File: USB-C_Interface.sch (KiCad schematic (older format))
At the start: 66 parts, among them IC3 TPS7A0518PDBVT, J12 WE_632723300011, J3 WE_632723300011, J4 WE_632723300011, U5 TPS25820DSST, U6 TS3USB30EDGSR, U7 TXB0104D, U8 CBTL02043ABQ,115, U9 FT232RQ-REEL

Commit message: Update power labels in USB2 seciton of USB sch, reorganize USB2 section
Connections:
- net labels added: 1V8_SYS, 3V3_SYS, 5V_SYS, VREG_S4A_1V8
- wire segments 309 -> 306
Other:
- moved on the sheet: C60, C61, C62, C63, C69, C70, C71, C72, C73, C74, C75, C80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

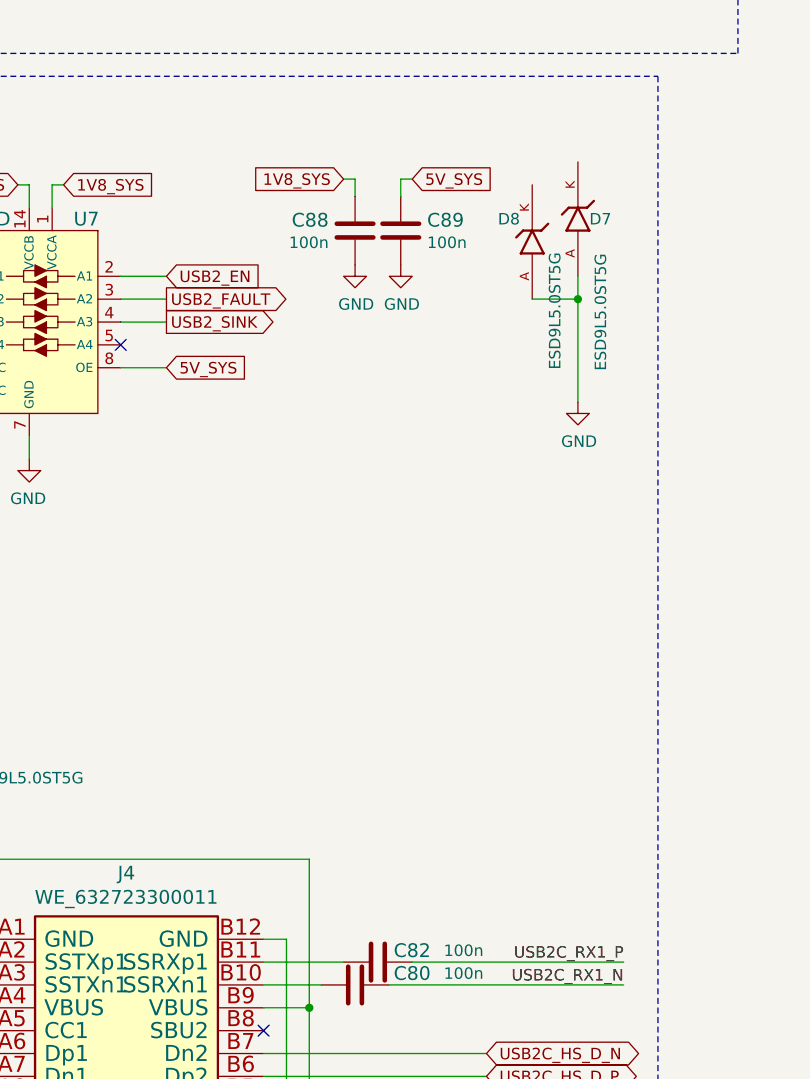
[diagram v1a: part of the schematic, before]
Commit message: Change U7 OE voltage to 1V8, change USB2.0 TSV to TPD4E05U06 to consolidate bom
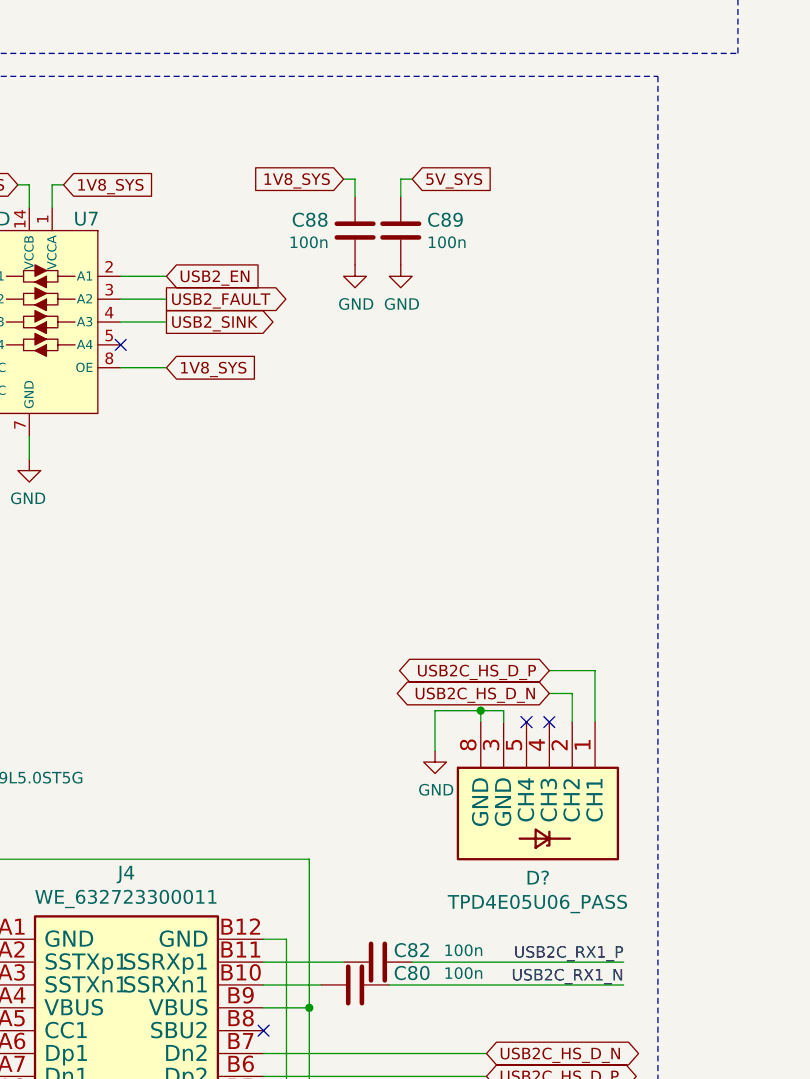
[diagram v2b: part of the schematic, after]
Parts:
- removed D7, D8: ESD9L5.0ST5G, sa800u-baseboard-hw-footprints:DIOM1006X40N, symbol sa800u-baseboard-hw:ESD9L5.0ST5G
- added D?: TPD4E05U06_PASS, sa800u-baseboard-hw-footprints:TPD4E05U06_PASS, symbol sa800u-baseboard-hw:TPD4E05U06_PASS
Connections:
- wire segments 306 -> 312
- no-connect marks 32 -> 34
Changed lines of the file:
@@
 Text Label 10700 9675 2    50   ~ 0
 USB2C_TX2_N
-$Comp
-L sa800u-baseboard-hw:ESD9L5.0ST5G D8
-U 1 1 62A14876
-P 10300 5725
-AR Path="/61A2F307/62A14876" Ref="D8"  Part="1"
-AR Path="/628CDA4A/62A14876" Ref="D?"  Part="1"
-F 0 "D8" V 10400 5875 50  0000 R CNN
-F 1 "ESD9L5.0ST5G" H 10255 5625 50  0000 R CNN
-F 2 "sa800u-baseboard-hw-footprints:DIOM1006X40N" H 10050 5925 50  0001 C CNN
-F 3 "https://www.farnell.com/datasheets/2353986.pdf" H 10300 5725 50  0001 C CNN
-F 4 "ESD9L5.0ST5G" H 10000 5975 50  0001 C CNN "MPN"
-F 5 "ONSEMI" H 10450 5975 50  0001 C CNN "Manufacturer"
-	1    10300 5725
-	0    -1   -1   0
-$EndComp
-$Comp
-L sa800u-baseboard-hw:ESD9L5.0ST5G D7
-U 1 1 62A1487E
-P 10500 5625
-AR Path="/61A2F307/62A1487E" Ref="D7"  Part="1"
-AR Path="/628CDA4A/62A1487E" Ref="D?"  Part="1"
-F 0 "D7" V 10500 5575 50  0000 R CNN
-F 1 "ESD9L5.0ST5G" H 10350 5525 50  0000 R CNN
-F 2 "sa800u-baseboard-hw-footprints:DIOM1006X40N" H 10250 5825 50  0001 C CNN
-F 3 "https://www.farnell.com/datasheets/2353986.pdf" H 10500 5625 50  0001 C CNN
-F 4 "ESD9L5.0ST5G" H 10200 5875 50  0001 C CNN "MPN"
-F 5 "ONSEMI" H 10650 5875 50  0001 C CNN "Manufacturer"
-	1    10500 5625
-	0    -1   -1   0
-$EndComp
-Wire Wire Line
-	10500 5875 10500 5975
-Wire Wire Line
-	10300 5975 10500 5975
-Connection ~ 10500 5975
-Wire Wire Line
-	10500 5975 10500 6425
-$Comp
-L sa800u-baseboard-hw:GND #PWR039
-U 1 1 62A1488A
-P 10500 6425
-AR Path="/61A2F307/62A1488A" Ref="#PWR039"  Part="1"
-AR Path="/628CDA4A/62A1488A" Ref="#PWR?"  Part="1"
-F 0 "#PWR039" H 10500 6175 50  0001 C CNN
-F 1 "GND" H 10505 6252 50  0000 C CNN
-F 2 "" H 10500 6425 50  0001 C CNN
-F 3 "" H 10500 6425 50  0001 C CNN
-	1    10500 6425
-	1    0    0    -1
-$EndComp
 Wire Wire Line
 	6975 9375 7925 9375
@@
 Wire Wire Line
 	8250 5475 8200 5475
-Text GLabel 8700 6275 2    50   Input ~ 0
-5V_SYS
 Text GLabel 8050 5475 0    50   Input ~ 0
 5V_SYS
@@
 Wire Wire Line
 	9475 5450 9525 5450
+Text GLabel 8700 6275 2    50   Input ~ 0
+1V8_SYS
+$Comp
+L sa800u-baseboard-hw:TPD4E05U06_PASS D?
+U 1 1 63DB6B08
+P 10375 8025
+AR Path="/61C01D88/63DB6B08" Ref="D?"  Part="1"
+AR Path="/61A2F307/63DB6B08" Ref="D?"  Part="1"
+F 0 "D?" V 10858 7975 60  0000 C CNN
+F 1 "TPD4E05U06_PASS" V 10964 7975 60  0000 C CNN
+F 2 "sa800u-baseboard-hw-footprints:TPD4E05U06_PASS" H 10375 8025 60  0001 C CNN
+F 3 "" H 10375 8025 60  0001 C CNN
+F 4 "Texas Instruments" H 10375 8025 50  0001 C CNN "Manufacturer"
+F 5 "TPD4E05U06DQAR" H 10375 8025 50  0001 C CNN "MPN"
+	1    10375 8025
+	0    1    1    0
+$EndComp
+Wire Wire Line
+	10175 7825 10175 7775
+Wire Wire Line
+	10175 7775 10075 7775
+Wire Wire Line
+	9875 7775 9875 7950
+Wire Wire Line
+	10075 7825 10075 7775
+Connection ~ 10075 7775
+Wire Wire Line
+	10075 7775 9875 7775
+$Comp
+L sa800u-baseboard-hw:GND #PWR?
+U 1 1 63DB6B14
+P 9875 7950
+AR Path="/61A60486/63DB6B14" Ref="#PWR?"  Part="1"
+AR Path="/61C01D88/63DB6B14" Ref="#PWR?"  Part="1"
+AR Path="/61A2F307/63DB6B14" Ref="#PWR?"  Part="1"
+F 0 "#PWR?" H 9875 7700 50  0001 C CNN
+F 1 "GND" H 9880 7777 50  0000 C CNN
+F 2 "" H 9875 7950 50  0001 C CNN
+F 3 "" H 9875 7950 50  0001 C CNN
+	1    9875 7950
+	1    0    0    -1
+$EndComp
+Wire Wire Line
+	10375 7700 10475 7700
+Wire Wire Line
+	10475 7700 10475 7825
+Wire Wire Line
+	10375 7600 10575 7600
+Wire Wire Line
+	10575 7600 10575 7825
+NoConn ~ 10375 7825
+NoConn ~ 10275 7825
+Text GLabel 10375 7600 0    50   BiDi ~ 0
+USB2C_HS_D_P
+Text GLabel 10375 7700 0    50   BiDi ~ 0
+USB2C_HS_D_N
 $EndSCHEMATC

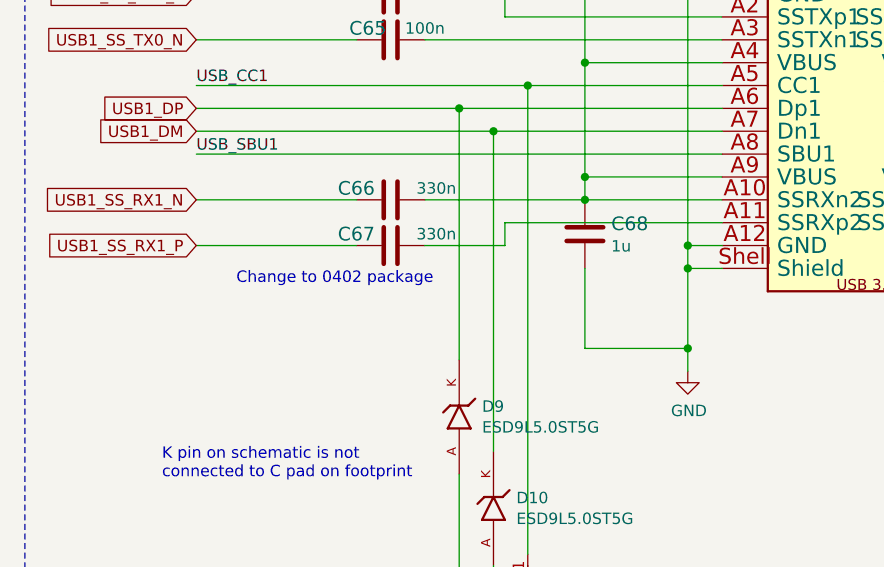
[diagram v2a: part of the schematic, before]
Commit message: Remove junction between USB1_SS_RX1_N and USB_VBUS
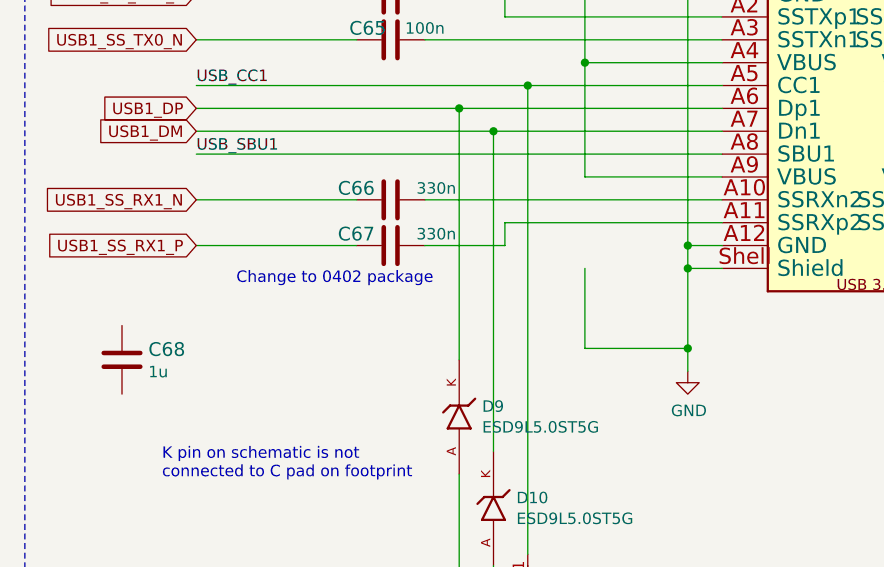
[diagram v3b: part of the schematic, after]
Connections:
- wire segments 312 -> 310
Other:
- moved on the sheet: C68
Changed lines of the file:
@@
 Wire Wire Line
 	5000 800  5000 1800
-$Comp
-L sa800u-baseboard-hw:C_1u_0402 C68
-U 1 1 61ACCBAB
-P 2950 2550
-F 0 "C68" H 3065 2595 60  0000 L CNN
-F 1 "C_1u_0402" H 2950 2400 60  0001 C CNN
-F 2 "sa800u-baseboard-hw-footprints:0402-cap" H 3150 2750 60  0001 L CNN
-F 3 "" H 2950 2550 50  0001 C CNN
-F 4 "TDK" H 3150 2950 60  0001 L CNN "Manufacturer"
-F 5 "C1005X6S1A105K050BC" H 3150 2850 60  0001 L CNN "MPN"
-F 6 "1u" H 3065 2497 50  0000 L CNN "Val"
-	1    2950 2550
-	1    0    0    -1
-$EndComp
 Wire Wire Line
 	3550 1800 2950 1800
@@
 	1    0    0    -1
 $EndComp
-Wire Wire Line
-	2950 2300 2950 2400
-Connection ~ 2950 2300
-Wire Wire Line
-	2950 2700 2950 3050
-Wire Wire Line
-	2950 3050 3400 3050
 Wire Wire Line
 	3550 1500 3400 1500
@@
 	1250 2200 3550 2200
 Wire Wire Line
-	3550 2400 2950 2400
-Connection ~ 2950 2400
-Wire Wire Line
-	2950 2400 2250 2400
-Wire Wire Line
 	3550 2500 2600 2500
 Wire Wire Line
@@
 Connection ~ 3400 2700
 Wire Wire Line
-	3400 2700 3400 3050
-Wire Wire Line
 	4800 2600 4800 3150
-Wire Wire Line
-	3400 3050 3400 3150
-Connection ~ 3400 3050
 $Comp
 L sa800u-baseboard-hw:TPD1E10B06DPYR D11
@@
 Text GLabel 10375 7700 0    50   BiDi ~ 0
 USB2C_HS_D_N
+Wire Wire Line
+	3400 3050 3400 3150
+Wire Wire Line
+	3400 2700 3400 3050
+Connection ~ 3400 3050
+Wire Wire Line
+	2950 3050 3400 3050
+Wire Wire Line
+	2950 2700 2950 3050
+$Comp
+L sa800u-baseboard-hw:C_1u_0402 C68
+U 1 1 61ACCBAB
+P 925 3100
+F 0 "C68" H 1040 3145 60  0000 L CNN
+F 1 "C_1u_0402" H 925 2950 60  0001 C CNN
+F 2 "sa800u-baseboard-hw-footprints:0402-cap" H 1125 3300 60  0001 L CNN
+F 3 "" H 925 3100 50  0001 C CNN
+F 4 "TDK" H 1125 3500 60  0001 L CNN "Manufacturer"
+F 5 "C1005X6S1A105K050BC" H 1125 3400 60  0001 L CNN "MPN"
+F 6 "1u" H 1040 3047 50  0000 L CNN "Val"
+	1    925  3100
+	1    0    0    -1
+$EndComp
+Wire Wire Line
+	2250 2400 3550 2400
 $EndSCHEMATC

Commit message: Update USB1 connector circuitry to match USB2, make it more readable
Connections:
- wire segments 310 -> 291
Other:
- note removed: "Change to 0402 package"
- moved on the sheet: C64, C65, C66, C67, C76, C77, C78, C79

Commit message: Update TSV diode on USB1, add second for VBUS and SBU signals
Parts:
- removed D10, D9: ESD9L5.0ST5G, sa800u-baseboard-hw-footprints:DIOM1006X40N, symbol sa800u-baseboard-hw:ESD9L5.0ST5G
- removed D11, D13: TPD1E10B06DPYR, sa800u-baseboard-hw-footprints:XDFN-2_1x0.60mm, symbol sa800u-baseboard-hw:TPD1E10B06DPYR
- added D? (x2): TPD4E05U06_PASS, sa800u-baseboard-hw-footprints:TPD4E05U06_PASS, symbol sa800u-baseboard-hw:TPD4E05U06_PASS
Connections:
- net labels added: USB1_CC1, USB1_CC2, USB1_SBU1, USB1_SBU2, USB_SBU1_EDP_AUX_N, USB_SBU2_EDP_AUX_P
- net labels removed: USB_CC1, USB_CC2
- wire segments 291 -> 315
- no-connect marks 34 -> 32
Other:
- note removed: "K pin on schematic is not \nconnected to C pad on footprint"
- moved on the sheet: C64, C65, C66, C67, C68, C76, C77, C78, C79, C84, C90, C91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

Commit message: Change USB switch, loclib
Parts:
- removed U6: TS3USB30EDGSR, sa800u-baseboard-hw-footprints:MSOP-10_W3mm, symbol sa800u-baseboard-hw:TS3USB30EDGSR
- added U?: FSUSB30MUX, sa800u-baseboard-hw-footprints:MSOP-10_W3mm, symbol sa800u-baseboard-hw:FSUSB30MUX
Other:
- moved on the sheet: R70

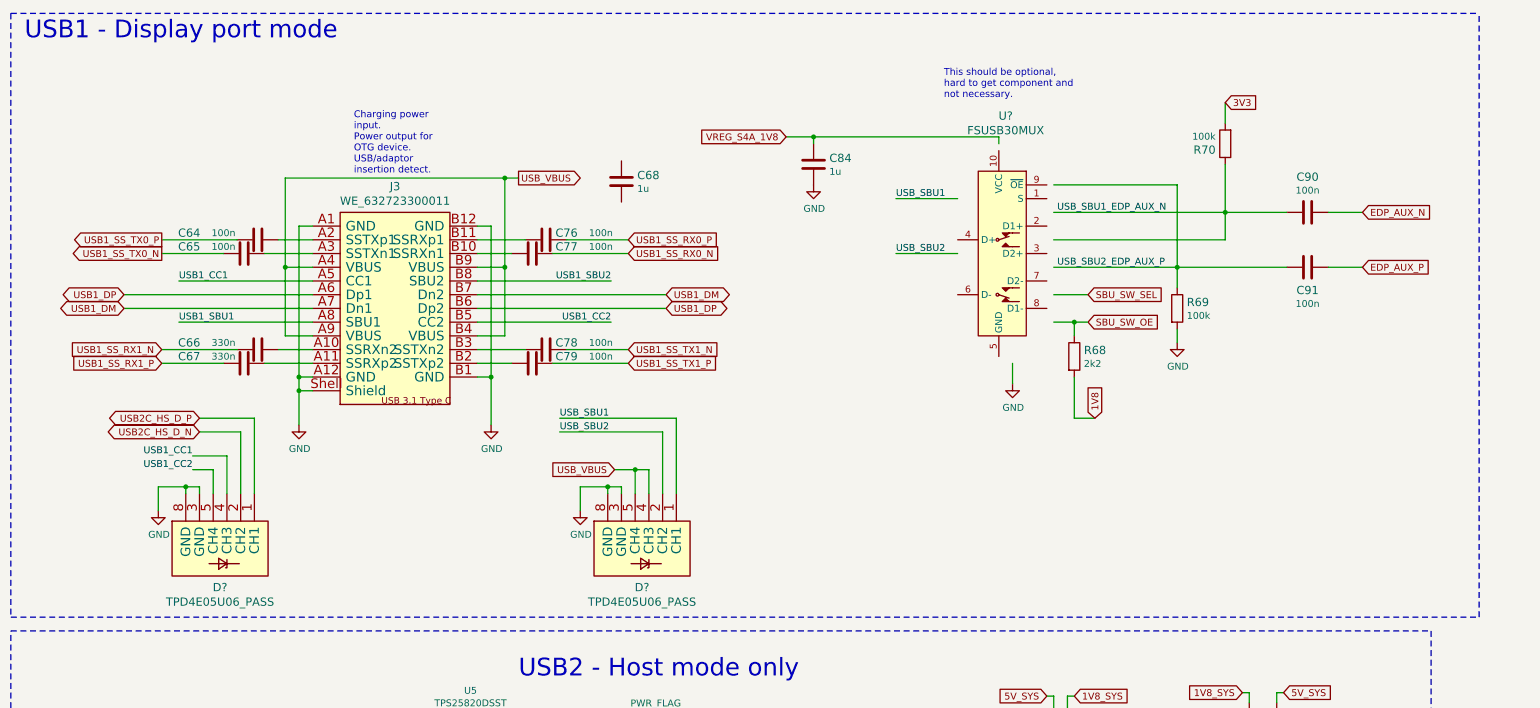
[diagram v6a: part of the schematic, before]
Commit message: Update FUSB30MUX symbol to clarify muxing
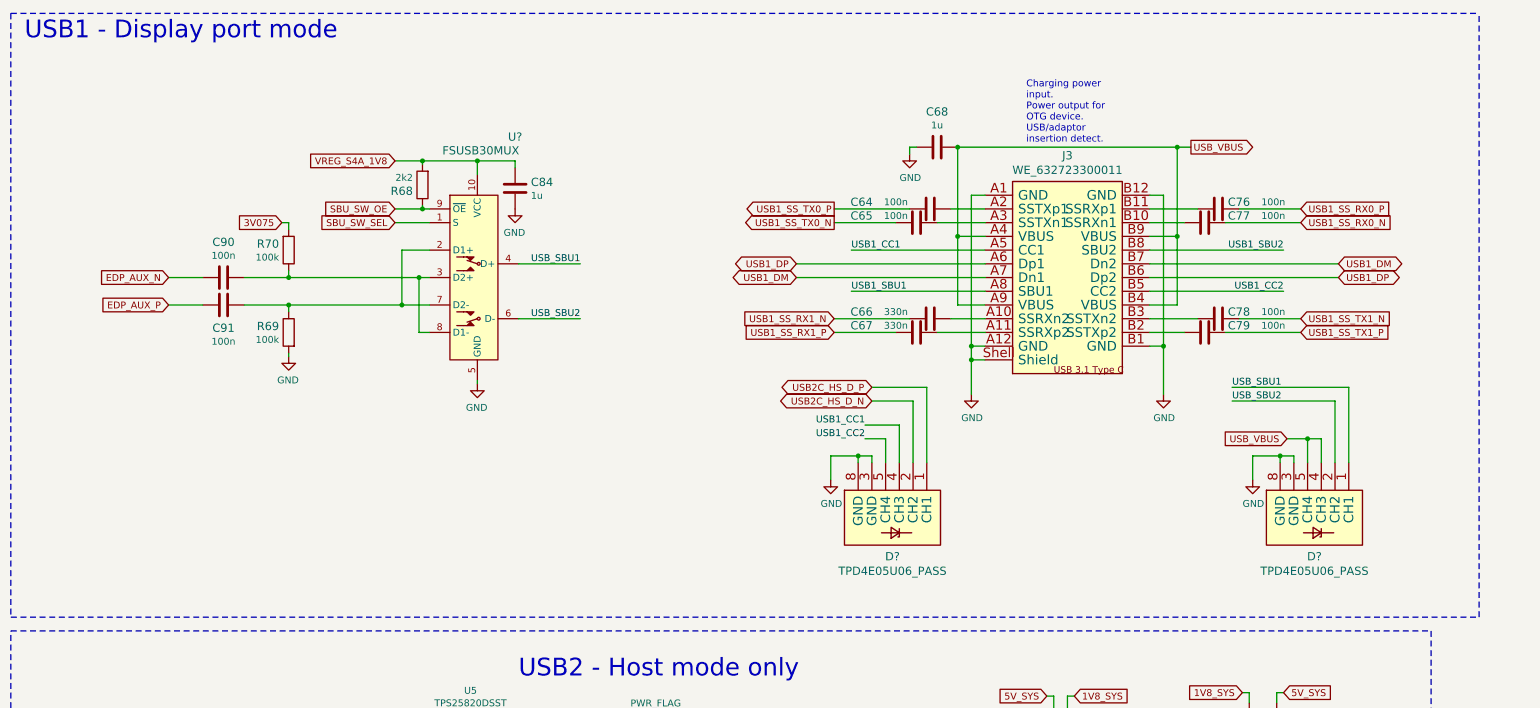
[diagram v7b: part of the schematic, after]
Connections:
- net labels added: 3V075
- net labels removed: 1V8, 3V3, USB_SBU1_EDP_AUX_N, USB_SBU2_EDP_AUX_P
- wire segments 315 -> 320
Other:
- note removed: "This should be optional,\nhard to get component and\nnot necessary."
- moved on the sheet: C64, C65, C66, C67, C68, C76, C77, C78, C79, C84, C90, C91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

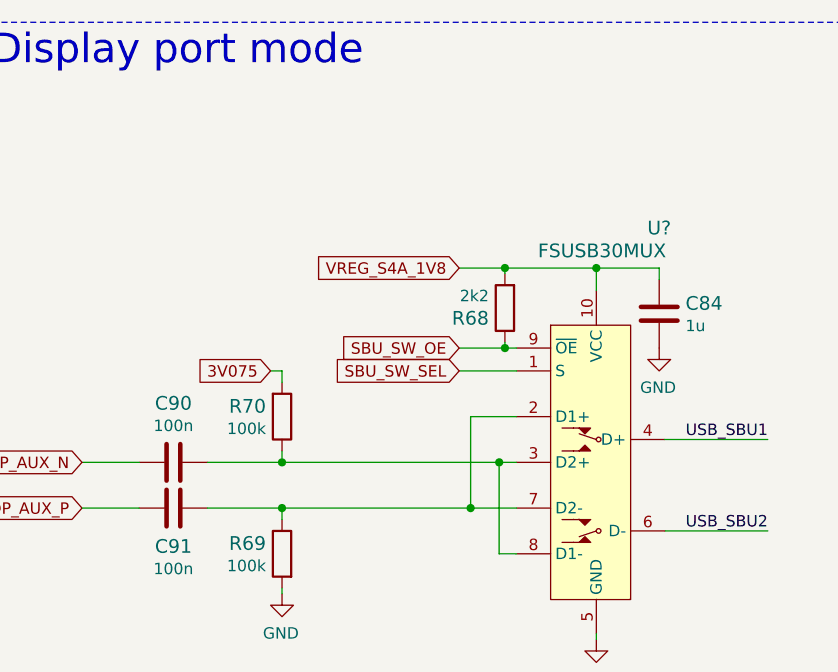
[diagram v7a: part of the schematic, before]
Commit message: Change SBU pullup voltage to 3V3_SYS
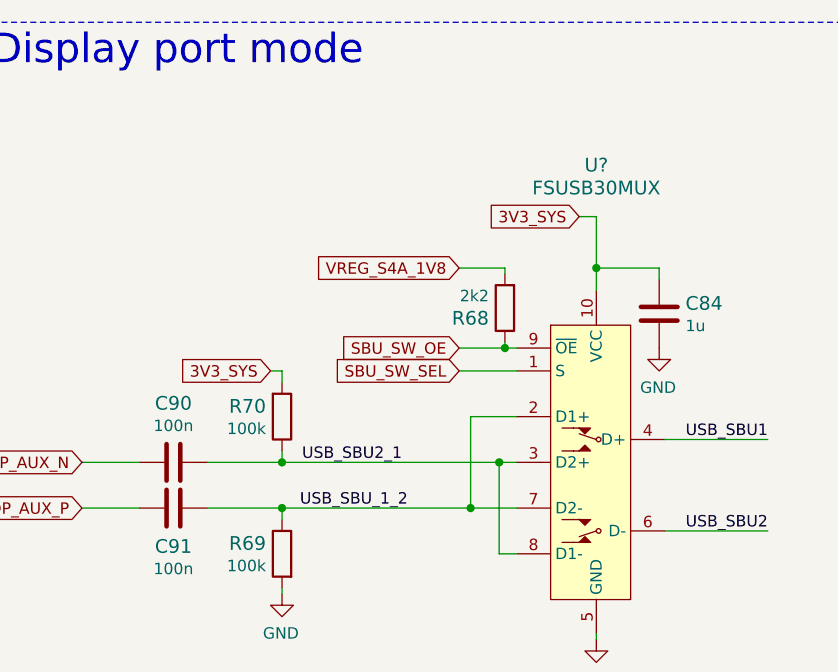
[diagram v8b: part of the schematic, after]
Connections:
- net 3V075 is gone; now on net 3V3_SYS: R70.2
- net 3V3_SYS: now also C84.1, U?.10 (VCC)
- net VREG_S4A_1V8: no longer C84.1, U?.10 (VCC)
- net USB_SBU_1_2: now reaches C91.2, R69.1, U?.2 (D1+), U?.7 (D2-)
- net USB_SBU2_1: now reaches C90.2, R70.1, U?.3 (D2+), U?.8 (D1-)
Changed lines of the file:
@@
 U 1 1 650075CA
 P 3900 2425
-F 0 "U?" H 4175 3450 60  0000 C CNN
-F 1 "FSUSB30MUX" H 3925 3350 60  0000 C CNN
+F 0 "U?" H 3900 3725 60  0000 C CNN
+F 1 "FSUSB30MUX" H 3900 3625 60  0000 C CNN
 F 2 "sa800u-baseboard-hw-footprints:MSOP-10_W3mm" H 4050 2615 60  0001 L CNN
 F 3 "" H 4050 2715 60  0001 L CNN
@@
 Text GLabel 3300 1575 0    50   Input ~ 0
 VREG_S4A_1V8
-Text GLabel 2475 2025 0    50   Input ~ 0
-3V075
 Text GLabel 3300 1925 0    50   Input ~ 0
 SBU_SW_OE
@@
 	3500 1600 3500 1575
 Wire Wire Line
-	3500 1575 3900 1575
-Connection ~ 3900 1575
-Wire Wire Line
 	3900 1575 3900 1675
 Wire Wire Line
@@
 Wire Wire Line
 	3300 1575 3500 1575
-Connection ~ 3500 1575
+Text GLabel 3825 1350 0    50   Input ~ 0
+3V3_SYS
+Wire Wire Line
+	3825 1350 3900 1350
+Wire Wire Line
+	3900 1350 3900 1575
+Connection ~ 3900 1575
+Text Label 3050 2425 2    50   ~ 0
+USB_SBU2_1
+Text Label 3075 2625 2    50   ~ 0
+USB_SBU_1_2
+Text GLabel 2475 2025 0    50   Input ~ 0
+3V3_SYS
 $EndSCHEMATC
